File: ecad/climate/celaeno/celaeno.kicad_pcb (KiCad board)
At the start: 2 copper layers, 80 x 45 mm, 73 parts, among them J1 MCV 1,5/ 2-G-3,5, J10 2.10mm ID, 5.5mm OD, J2 MCV 1,5/ 2-G-3,5, J3 5566-02A, J4 M20-8760342, J5 47053-1000, J6 47053-1000, J7 2.10mm ID, 5.5mm OD, J8 6410-02A, J9 6410-02A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

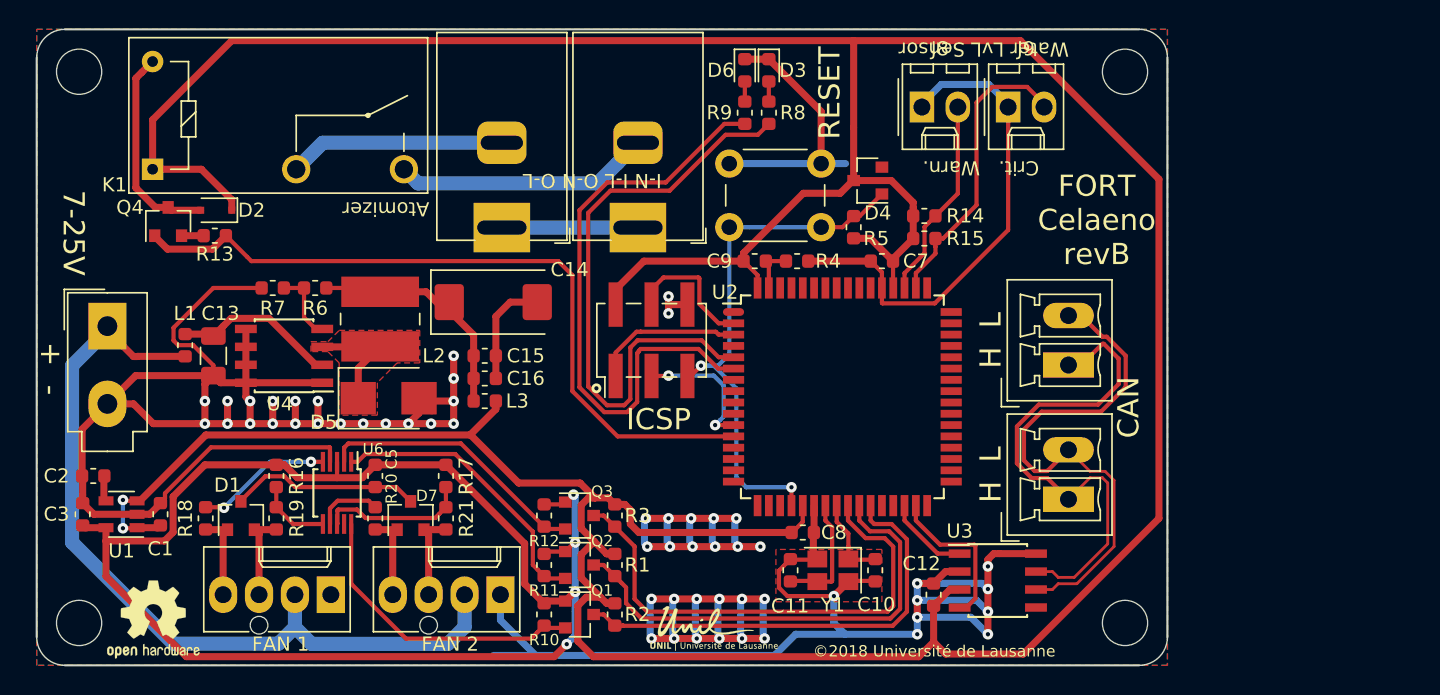
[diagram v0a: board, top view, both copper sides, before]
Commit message: Adds optional library of spice components
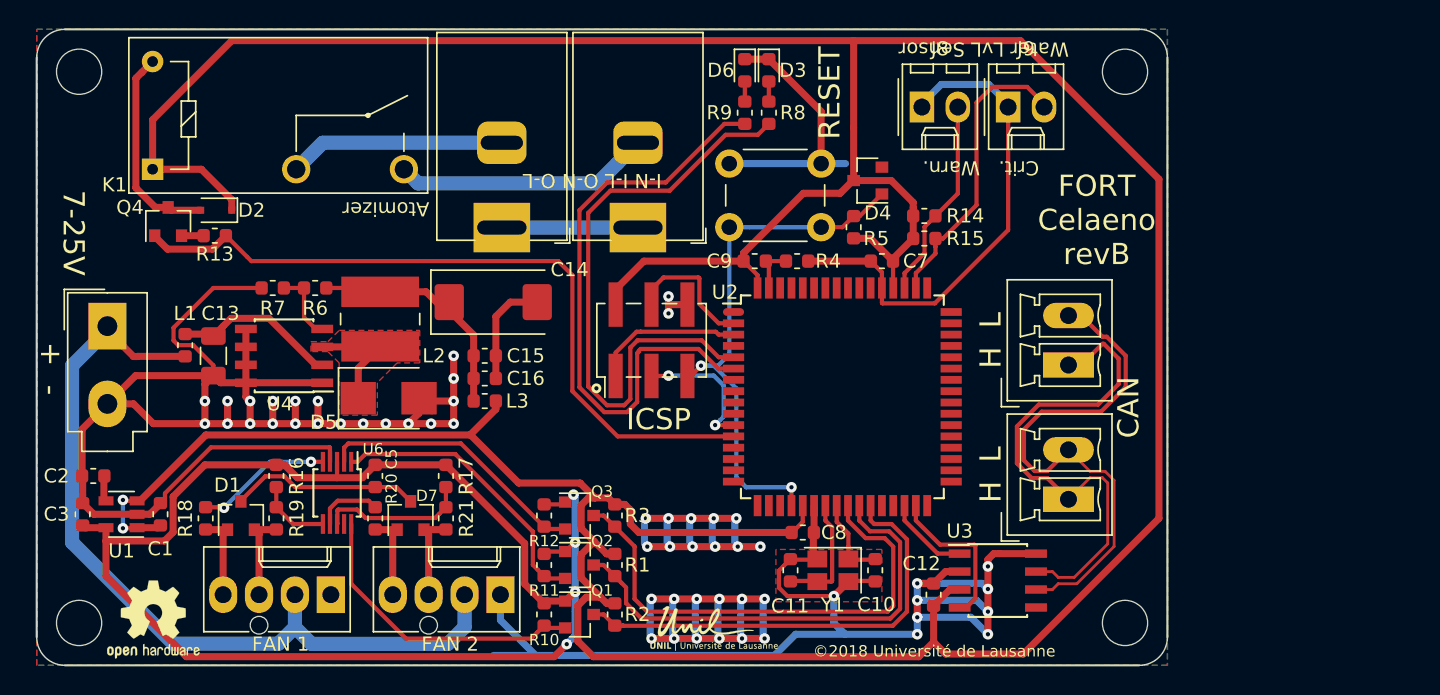
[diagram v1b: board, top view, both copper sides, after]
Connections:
- net /Fan PWM Controller 1/~ALERT renamed /Fan PWM Controller 1/~{ALERT}
- net /UC/~FAN_ALERT renamed /UC/~{FAN_ALERT}
- net /UC/~ICSP_RESET renamed /UC/~{ICSP_RESET}
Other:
- net class 24VAC removed
- net class Default removed
- net class Power removed

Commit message: [WIP] Updating Celaeno to new connector and SSR
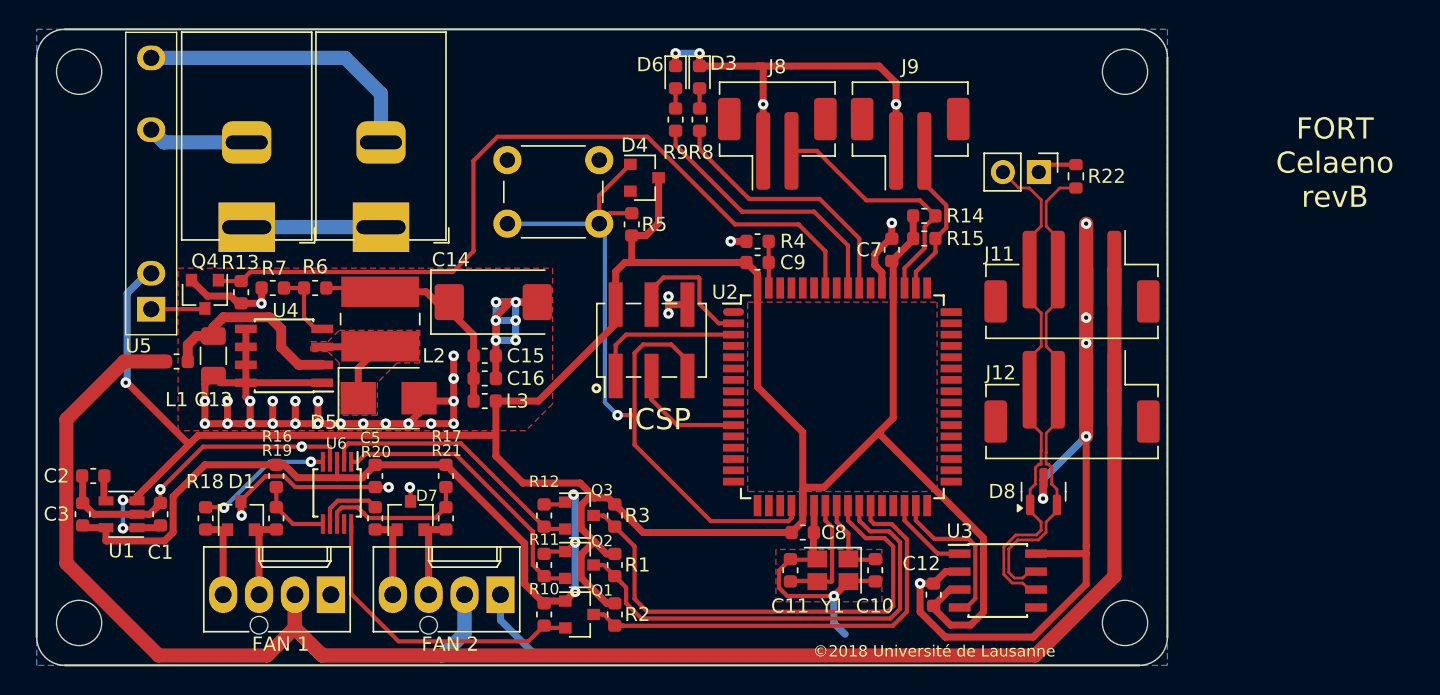
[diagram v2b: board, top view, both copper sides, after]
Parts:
- removed D2: 1N4148WS, Diode_SMD:D_SOD-323F
- removed G***: LOGO, FORT:UNIL-LOGO_9.2x3
- removed J1, J2: MCV 1,5/ 2-G-3,5, Connector_Phoenix_MC:PhoenixContact_MCV_1,5_2-G-3.5_1x02_P3.50mm_Vertical
- removed J3: 5566-02A, Connector_Molex:Molex_Mini-Fit_Jr_5566-02A_2x01_P4.20mm_Vertical
- removed K1: G5Q-1A4-EU DC5, Relay_THT:Relay_SPST_Omron-G5Q-1A
- removed the REF** at (128.2, 126.8)
- added D8: ESD752DBZR, Package_TO_SOT_SMD:SOT-23, F.Cu at (191.2, 117.7)
- added J11: JST SH, FORT:JST_PH_B4B-PH-SM4-TB_1x04-1MP_P2.00mm_Vertical, F.Cu at (193.2, 102.5)
- added J12: JST SH, FORT:JST_PH_B4B-PH-SM4-TB_1x04-1MP_P2.00mm_Vertical, F.Cu at (193.2, 111.0)
- added JP1: Term, Connector_PinHeader_2.54mm:PinHeader_1x02_P2.54mm_Vertical, F.Cu at (190.9, 95.1)
- added R22: 120, Resistor_SMD:R_0603_1608Metric, F.Cu at (193.5, 95.4)
- added U5: CPC1966YX6, FORT:SIP4_LittleFuse_CPC19X6yX6, F.Cu at (128.1, 95.9)
- C10, C11: value 18pF -> 18p
- J8, J9: footprint Connector_Molex:Molex_KK-254_AE-6410-02A_1x02_P2.54mm_Vertical -> Connector_JST:JST_PH_B2B-PH-SM4-TB_1x02-1MP_P2.00mm_Vertical
- moved J7 27.7 mm to (134.9, 99.0)
- moved D4 15.8 mm to (163.0, 95.5), turned to 0 degrees
- moved SW1 15.7 mm to (153.3, 94.2)
- moved R5 15.7 mm to (162.1, 98.8)
- moved J8 10.6 mm to (172.4, 93.1)
- moved J10 8.55 mm to (144.4, 99.0)
- moved J9 7.40 mm to (181.8, 93.1)
- moved Q4 5.77 mm to (131.9, 103.8), turned to -90 degrees
- moved D3 4.92 mm to (166.9, 88.4)
- moved D6 4.92 mm to (165.2, 88.4)
- moved R8 4.92 mm to (166.9, 91.4)
- moved R9 4.92 mm to (165.2, 91.4)
- moved R13 4.41 mm to (134.5, 103.6), turned to 90 degrees
- moved R4 3.13 mm to (171.0, 100.0), turned to 180 degrees
- moved L1 1.30 mm to (129.9, 108.5), turned to 180 degrees
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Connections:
- net /UC/CAN_RX renamed /CAN Transceiver/RXD
- net /UC/CAN_TX renamed /CAN Transceiver/TXD
- net /UC/~{FAN_ALERT} renamed /I2C Level Shifter/~{INT_5V}
- U2 pad 1: (no net) -> unconnected-(U2-NC-Pad1)
- U2 pad 10: (no net) -> unconnected-(U2-PB0-Pad10)
- U2 pad 12: /Relay/CMD -> unconnected-(U2-PB2-Pad12)
- U2 pad 13: (no net) -> unconnected-(U2-PB3-Pad13)
- U2 pad 14: (no net) -> unconnected-(U2-PB4-Pad14)
- U2 pad 15: (no net) -> unconnected-(U2-PB5-Pad15)
- U2 pad 16: (no net) -> unconnected-(U2-PB6-Pad16)
- U2 pad 17: (no net) -> unconnected-(U2-PB7-Pad17)
- U2 pad 18: (no net) -> unconnected-(U2-PG3-Pad18)
- U2 pad 19: (no net) -> unconnected-(U2-PG4-Pad19)
- U2 pad 28: (no net) -> unconnected-(U2-PD3-Pad28)
- U2 pad 29: (no net) -> unconnected-(U2-PD4-Pad29)
- U2 pad 32: (no net) -> unconnected-(U2-PD7-Pad32)
- U2 pad 33: (no net) -> unconnected-(U2-PG0-Pad33)
- U2 pad 34: (no net) -> unconnected-(U2-PG1-Pad34)
- U2 pad 35: (no net) -> unconnected-(U2-PC0-Pad35)
- U2 pad 36: (no net) -> unconnected-(U2-PC1-Pad36)
- U2 pad 37: (no net) -> unconnected-(U2-PC2-Pad37)
- U2 pad 38: (no net) -> unconnected-(U2-PC3-Pad38)
- U2 pad 39: (no net) -> unconnected-(U2-PC4-Pad39)
- U2 pad 4: (no net) -> unconnected-(U2-PE2-Pad4)
- U2 pad 40: (no net) -> unconnected-(U2-PC5-Pad40)
- U2 pad 41: (no net) -> unconnected-(U2-PC6-Pad41)
- U2 pad 42: (no net) -> unconnected-(U2-PC7-Pad42)
- U2 pad 43: (no net) -> unconnected-(U2-PG2-Pad43)
- U2 pad 44: (no net) -> unconnected-(U2-PA7-Pad44)
- U2 pad 45: (no net) -> unconnected-(U2-PA6-Pad45)
- U2 pad 46: (no net) -> unconnected-(U2-PA5-Pad46)
- U2 pad 47: (no net) -> unconnected-(U2-PA4-Pad47)
- U2 pad 48: (no net) -> unconnected-(U2-PA3-Pad48)
- U2 pad 49: (no net) -> unconnected-(U2-PA2-Pad49)
- U2 pad 5: /UC/LED_GREEN -> unconnected-(U2-PE3-Pad5)
- U2 pad 54: (no net) -> unconnected-(U2-PF7-Pad54)
- U2 pad 55: (no net) -> /UC/LED_GREEN
- U2 pad 56: (no net) -> /UC/LED_YELLOW
- U2 pad 57: (no net) -> unconnected-(U2-PF4-Pad57)
- U2 pad 58: (no net) -> /Relay/CMD
- U2 pad 59: (no net) -> unconnected-(U2-PF2-Pad59)
- U2 pad 6: /UC/LED_YELLOW -> unconnected-(U2-PE4-Pad6)
- U2 pad 60: (no net) -> unconnected-(U2-PF1-Pad60)
- U2 pad 61: (no net) -> unconnected-(U2-PF0-Pad61)
- U2 pad 62: (no net) -> unconnected-(U2-AREF-Pad62)
- U2 pad 7: (no net) -> unconnected-(U2-PE5-Pad7)
- U2 pad 8: (no net) -> unconnected-(U2-PE6-Pad8)
- U2 pad 9: (no net) -> unconnected-(U2-PE7-Pad9)
- U3 pad 5: (no net) -> unconnected-(U3-SPLIT-Pad5)
- U3 pad 6: /CAN Transceiver/CAN- -> /CAN-
- U3 pad 7: /CAN Transceiver/CAN+ -> /CAN+
- U6 pad 9: (no net) -> unconnected-(U6-CLK-Pad9)
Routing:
- net +5V: track 291.4 -> 189.2 mm, vias 2 -> 3
- net GND: track 330.3 -> 238.2 mm, vias 55 -> 48
- net +12V: track 59.9 -> 144.8 mm
- net +3V3: track 102.1 -> 60.3 mm, vias 4 -> 3
- net /CAN Transceiver/CAN-: track 37.7 -> 0.00 mm
- net /CAN-: track 0.00 -> 36.8 mm
- net /CAN Transceiver/CAN+: track 36.3 -> 0.00 mm
- net /CAN+: track 0.00 -> 35.1 mm
- net /UC/LED_GREEN: track 43.1 -> 18.7 mm
- net /UC/LED_YELLOW: track 42.9 -> 19.2 mm
- net /UC/~{ICSP_RESET}: track 39.4 -> 56.0 mm, vias 2 -> 1
- net /Relay/A: track 18.2 -> 7.13 mm
- net Net-(Q4-D): track 14.7 -> 3.82 mm
- net /UC/LVL_1: track 21.2 -> 11.2 mm
- net /Relay/B: track 15.3 -> 20.8 mm
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- added copper zone on F.Cu, net +5V
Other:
- board text removed: "+ -"
- board text removed: "7-25V"
- board text removed: "Atomizer"
- board text removed: "CAN"
- board text removed: "Crit. Warn."
- board text removed: "H L"
- board text removed: "I-N I-L O-N O-L"
- board text removed: "RESET"
- board text removed: "Water LvL Sensor"

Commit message: Updates Celaeno to new connector
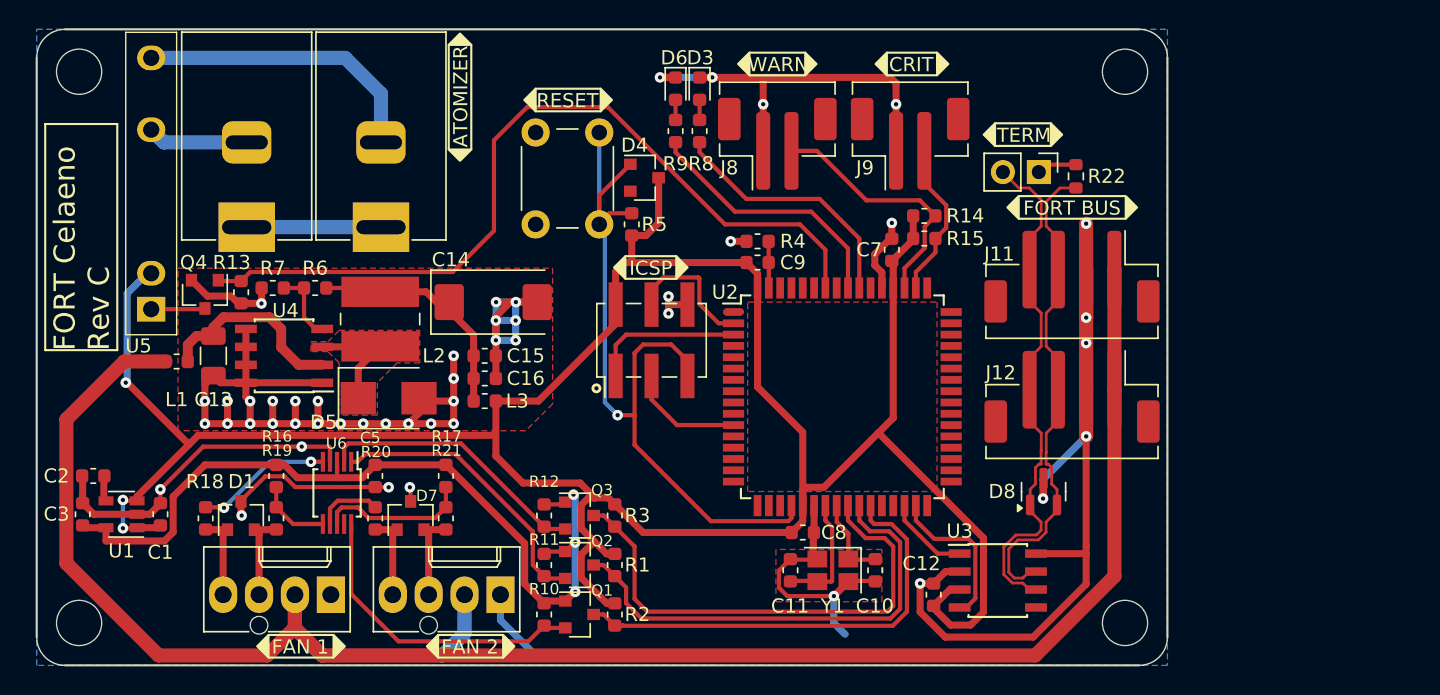
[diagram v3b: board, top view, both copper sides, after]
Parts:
- J11, J12: value JST SH -> JST PH
- J8, J9: value 6410-02A -> JST PH; footprint Connector_JST:JST_PH_B2B-PH-SM4-TB_1x02-1MP_P2.00mm_Vertical -> FORT:JST_PH_B2B-PH-SM4-TB_1x02-1MP_P2.00mm_Vertical
- moved SW1 4.97 mm to (155.3, 98.8), turned to 90 degrees
- moved D3 0.81 mm to (166.9, 89.2)
- moved D6 0.81 mm to (165.2, 89.2)
- moved R8 0.81 mm to (166.9, 92.2)
- moved R9 0.81 mm to (165.2, 92.2)
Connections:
- net /UC/LVL_0 renamed /UC/LVL_WARN
- net /UC/LVL_1 renamed /UC/LVL_CRIT
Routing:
- net /Relay/CMD: track 56.9 -> 58.7 mm
- net /UC/LED_GREEN: track 18.7 -> 18.0 mm
- net /UC/LED_YELLOW: track 19.2 -> 18.5 mm
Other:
- board text added: "ATOMIZER"
- board text added: "CRIT"
- board text added: "FORT BUS"
- board text added: "FORT Celaeno Rev C"
- board text added: "RESET"
- board text added: "TERM"
- board text added: "WARN"
- board text added: "©2018 Université de Lausanne ©2024 Université de Genève"
- board text removed: "FORT Celaeno revB"
- board text removed: "©2018 Université de Lausanne"

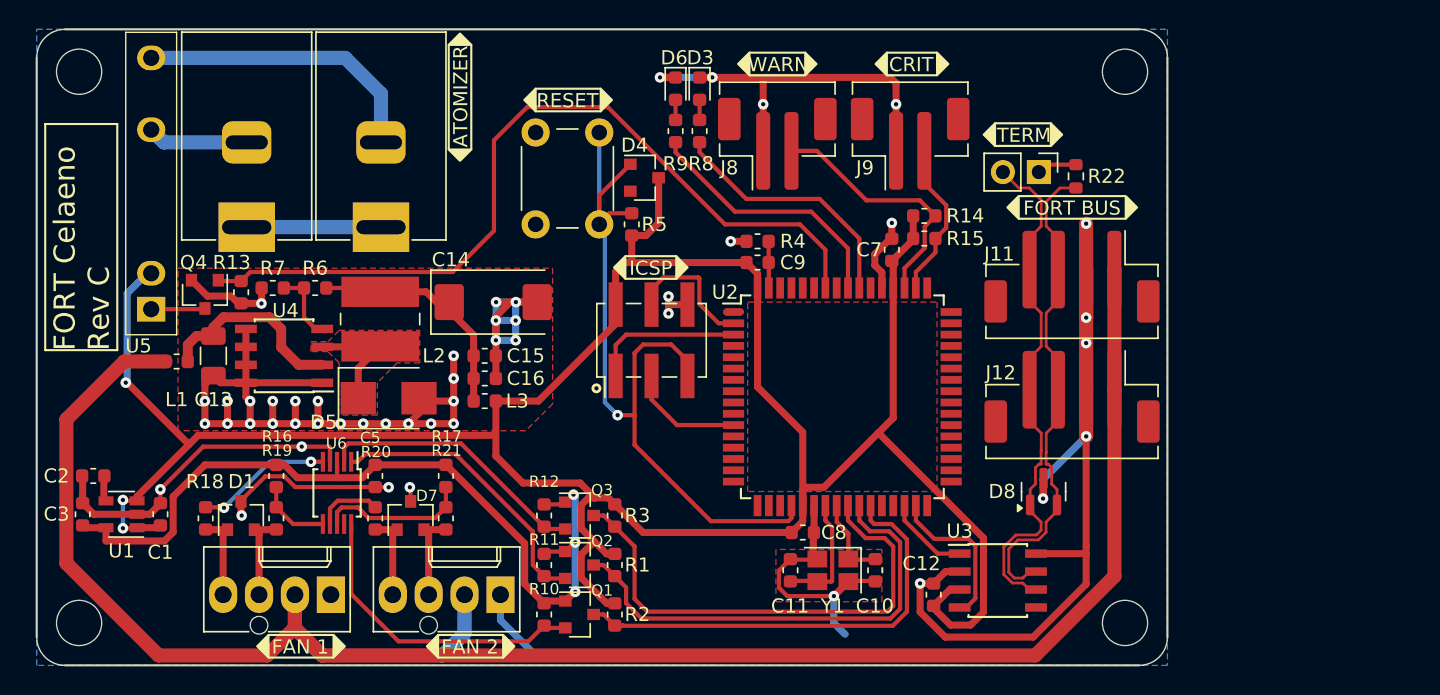
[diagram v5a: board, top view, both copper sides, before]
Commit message: Fixes Manufacturing data
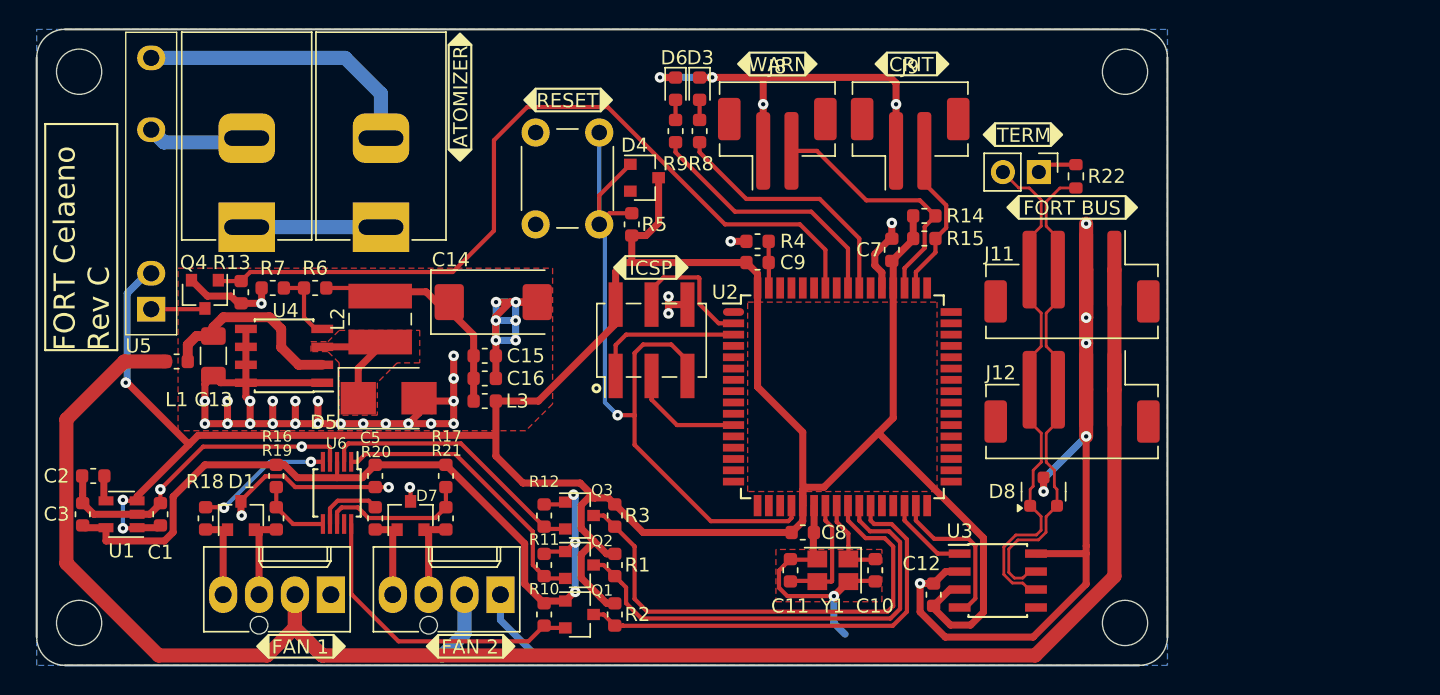
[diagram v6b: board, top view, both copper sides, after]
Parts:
- C1, C3: value 1uF -> 1u
- C2: value 10nF -> 10n
- D8: value ESD752DBZR -> CDSOT23-T24CAN
- J8, J9: footprint FORT:JST_PH_B2B-PH-SM4-TB_1x02-1MP_P2.00mm_Vertical -> Connector_JST:JST_PH_B2B-PH-SM4-TB_1x02-1MP_P2.00mm_Vertical
- L2: footprint Inductor_SMD:L_Wuerth_WE-PD2-Typ-MS -> FORT:L_Wuerth_WE-PD2
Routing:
- net GND: track 238.4 -> 237.3 mm

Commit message: Updates PCBs
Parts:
- J8, J9: footprint Connector_JST:JST_PH_B2B-PH-SM4-TB_1x02-1MP_P2.00mm_Vertical -> FORT:JST_PH_B2B-PH-SM4-TB_1x02-1MP_P2.00mm_Vertical
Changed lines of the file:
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@@
 			(pintype "passive")
 		)
-		(model "${KIPRJMOD}/../../lib/fort.3dshapes/47053-1000.wrl"
+		(model "${KIPRJMOD}/lib/fort.3dshapes/47053-1000.step"
 			(offset
 				(xyz 0 0 0)
@@
 			(pintype "passive")
 		)
-		(model "${KIPRJMOD}/../../lib/fort.3dshapes/47053-1000.wrl"
+		(model "${KIPRJMOD}/lib/fort.3dshapes/47053-1000.step"
 			(offset
 				(xyz 0 0 0)
@@
 		)
 	)
-	(footprint "Connector_JST:JST_PH_B2B-PH-SM4-TB_1x02-1MP_P2.00mm_Vertical"
+	(footprint "FORT:JST_PH_B2B-PH-SM4-TB_1x02-1MP_P2.00mm_Vertical"
 		(layer "F.Cu")
 		(at 181.8 93.1)
@@
 			)
 		)
-		(property "Footprint" "Connector_JST:JST_PH_B2B-PH-SM4-TB_1x02-1MP_P2.00mm_Vertical"
+		(property "Footprint" "FORT:JST_PH_B2B-PH-SM4-TB_1x02-1MP_P2.00mm_Vertical"
 			(at 0 0 0)
 			(unlocked yes)
@@
 			(roundrect_rratio 0.15625)
 		)
-		(model "${KICAD8_3DMODEL_DIR}/Connector_JST.3dshapes/JST_PH_B2B-PH-SM4-TB_1x02-1MP_P2.00mm_Vertical.wrl"
+		(model "${KIPRJMOD}/lib/fort.3dshapes/B2B-PH-SM4-TB.step"
 			(offset
-				(xyz 0 0 0)
+				(xyz 0 1.75 0)
 			)
 			(scale
@@
 			)
 			(rotate
-				(xyz 0 0 0)
+				(xyz -90 0 0)
 			)
 		)
 	)
-	(footprint "Connector_JST:JST_PH_B2B-PH-SM4-TB_1x02-1MP_P2.00mm_Vertical"
+	(footprint "FORT:JST_PH_B2B-PH-SM4-TB_1x02-1MP_P2.00mm_Vertical"
 		(layer "F.Cu")
 		(at 172.4 93.1)
@@
 			)
 		)
-		(property "Footprint" "Connector_JST:JST_PH_B2B-PH-SM4-TB_1x02-1MP_P2.00mm_Vertical"
+		(property "Footprint" "FORT:JST_PH_B2B-PH-SM4-TB_1x02-1MP_P2.00mm_Vertical"
 			(at 0 0 0)
 			(unlocked yes)
@@
 			(roundrect_rratio 0.15625)
 		)
-		(model "${KICAD8_3DMODEL_DIR}/Connector_JST.3dshapes/JST_PH_B2B-PH-SM4-TB_1x02-1MP_P2.00mm_Vertical.wrl"
+		(model "${KIPRJMOD}/lib/fort.3dshapes/B2B-PH-SM4-TB.step"
 			(offset
-				(xyz 0 0 0)
+				(xyz 0 1.75 0)
 			)
 			(scale
@@
 			)
 			(rotate
-				(xyz 0 0 0)
+				(xyz -90 0 0)
 			)
 		)

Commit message: Flatten Arke schematics
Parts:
- added R23: 220, Resistor_SMD:R_0603_1608Metric, F.Cu at (125.3, 105.6)
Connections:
- U5 pad 1: Net-(Q4-D) -> Net-(R23-Pad2)
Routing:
- net Net-(Q4-D): track 3.82 -> 7.29 mm
- net Net-(R23-Pad2): track 0.00 -> 2.81 mm
